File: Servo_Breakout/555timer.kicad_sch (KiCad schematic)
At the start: 14 parts, among them U501 ICM7555xP, U502 TPL0401A-10-Q1

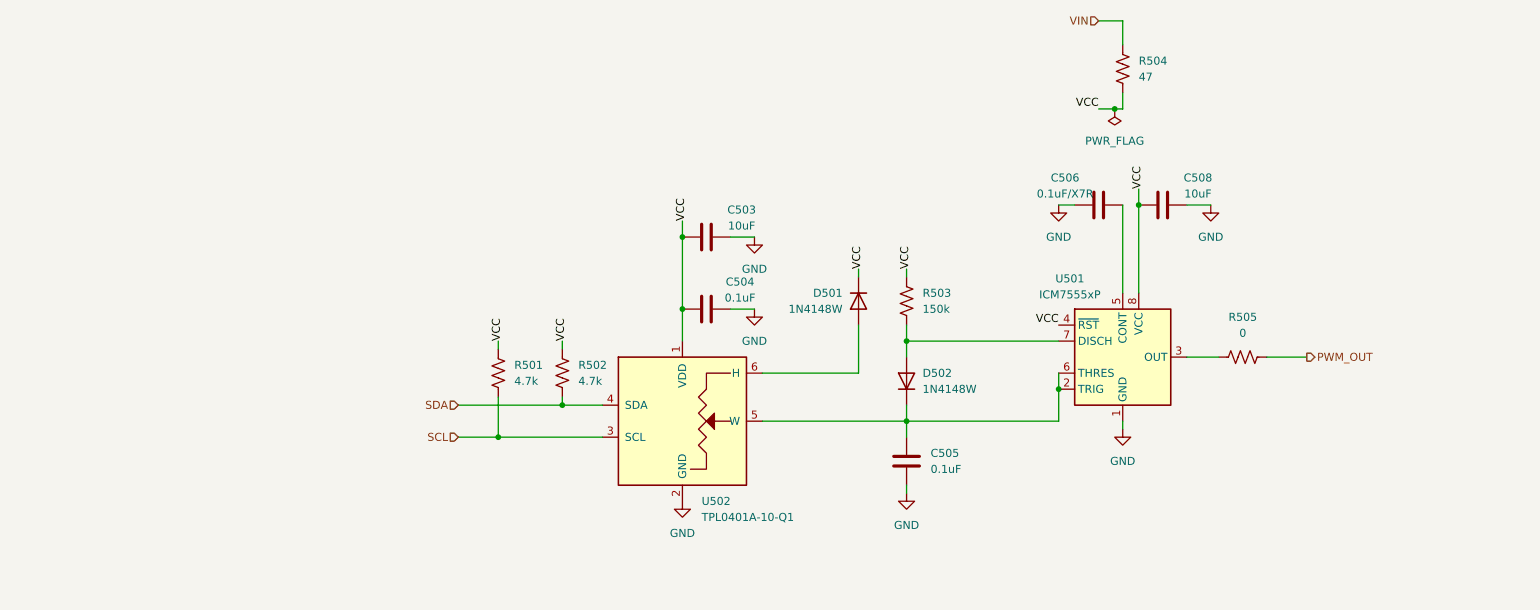
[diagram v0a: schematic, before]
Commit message: simplify 555 timer circuit. update green_led switch to low-side switching
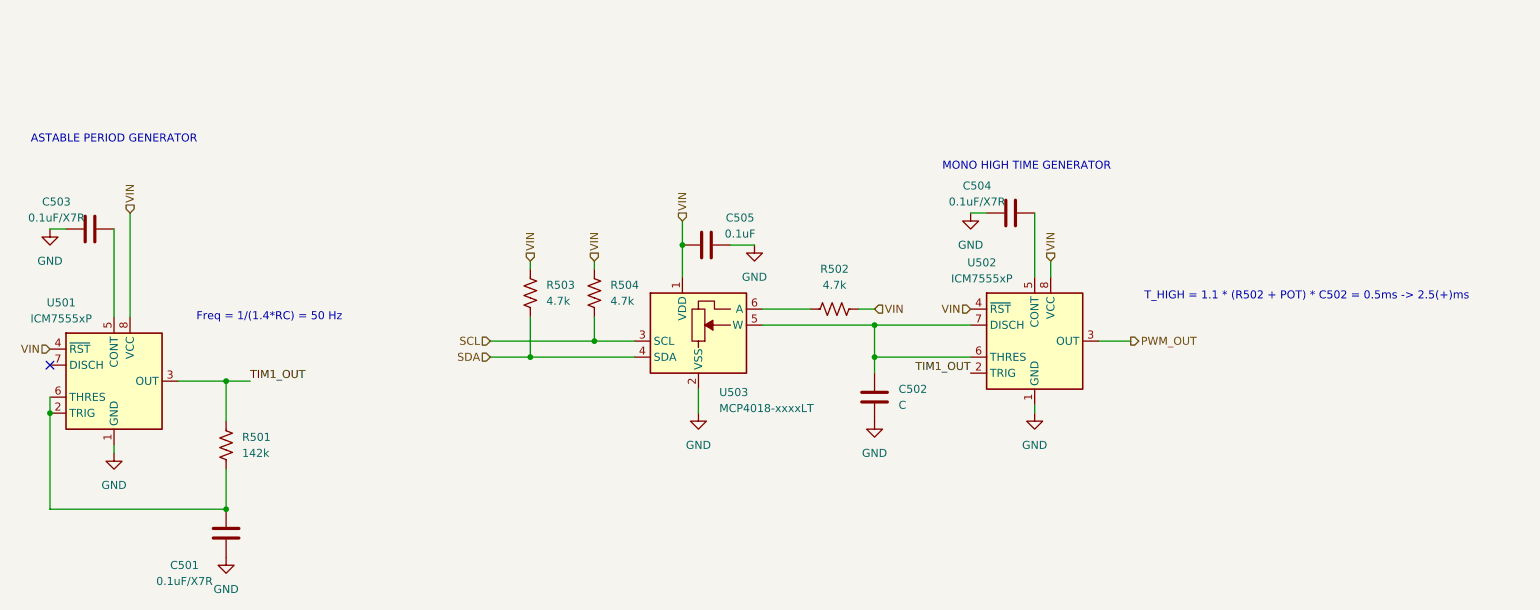
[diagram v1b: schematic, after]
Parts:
- removed C503, C508: 10uF, Capacitor_SMD:C_0805_2012Metric_Pad1.18x1.45mm_HandSolder, symbol Device:C
- removed C505: 0.1uF, Capacitor_SMD:C_0805_2012Metric_Pad1.18x1.45mm_HandSolder, symbol Device:C
- removed D501, D502: 1N4148W, Diode_SMD:D_SOD-123, symbol Diode:1N4148W
- removed R503: 150k, Resistor_SMD:R_0805_2012Metric_Pad1.20x1.40mm_HandSolder, symbol Device:R_US
- removed R504: 47, Resistor_SMD:R_0805_2012Metric_Pad1.20x1.40mm_HandSolder, symbol Device:R_US
- removed R505: 0, Resistor_SMD:R_0603_1608Metric, symbol Device:R_US
- removed U502: TPL0401A-10-Q1, Package_TO_SOT_SMD:Texas_R-PDSO-G6, symbol Potentiometer_Digital:TPL0401A-10-Q1
- added C501, C504: 0.1uF/X7R, Capacitor_SMD:C_0805_2012Metric_Pad1.18x1.45mm_HandSolder, symbol Device:C
- added C502: C, symbol Device:C
- added R501: 142k, symbol Device:R_US
- added R502: 4.7k, symbol Device:R_US
- added U502: ICM7555xP, Package_DIP:DIP-8_W7.62mm, symbol Timer:ICM7555xP
- added U503: MCP4018-xxxxLT, Package_TO_SOT_SMD:SOT-363_SC-70-6, symbol Potentiometer_Digital:MCP4018-xxxxLT
- renumbered C506 to C503, C504 to C505, R501 to R503, R502 to R504
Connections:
- net VCC is gone; now on net VIN: C505.1, R503.1, R504.1, U501.4 (~{RST}), U501.8 (VCC)
- net GND: now also C501.2, C502.2, C504.2, U502.1 (GND), U503.2 (VSS)
- net PWM_OUT: now also U502.3 (OUT)
- net SCL: now also R504.2, U503.3 (SCL); no longer R503.2
- net SDA: now also R503.2, U503.4 (SDA); no longer R504.2
- net VIN: now also R502.2, U502.4 (~{RST}), U502.8 (VCC), U503.1 (VDD)
- net at U501.2 (TRIG), U501.6 (THRES): now also C501.1, R501.2
- net TIM1_OUT: now reaches U501.3 (OUT)
- net TIM1_OUT: now also R501.1, U502.2 (TRIG)
- new net: R502.1, U503.6 (A)
- new net: C502.1, U502.6 (THRES), U502.7 (DISCH), U503.5 (W)
- new net: C504.1, U502.5 (CONT)
- no-connect marks 0 -> 1
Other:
- note added: "ASTABLE PERIOD GENERATOR"
- note added: "Freq = 1/(1.4*RC) = 50 Hz"
- note added: "MONO HIGH TIME GENERATOR"
- note added: "T_HIGH = 1.1 * (R502 + POT) * C502 = 0.5ms -> 2.5(+)ms"
- moved on the sheet: C503, C505, R503, R504, U501

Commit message: completed layout rework for two 555 timers
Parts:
- C502: footprint (none) -> Capacitor_SMD:C_0805_2012Metric_Pad1.18x1.45mm_HandSolder
- R501, R502: footprint (none) -> Resistor_SMD:R_0805_2012Metric_Pad1.20x1.40mm_HandSolder
- R503, R504: footprint Resistor_SMD:R_0603_1608Metric -> Resistor_SMD:R_0805_2012Metric_Pad1.20x1.40mm_HandSolder
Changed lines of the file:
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@@
 			)
 		)
-		(property "Footprint" ""
+		(property "Footprint" "Resistor_SMD:R_0805_2012Metric_Pad1.20x1.40mm_HandSolder"
 			(at 155.194 89.154 90)
 			(effects
@@
 			)
 		)
-		(property "Footprint" "Resistor_SMD:R_0603_1608Metric"
+		(property "Footprint" "Resistor_SMD:R_0805_2012Metric_Pad1.20x1.40mm_HandSolder"
 			(at 107.696 87.884 90)
 			(effects
@@
 			)
 		)
-		(property "Footprint" "Resistor_SMD:R_0603_1608Metric"
+		(property "Footprint" "Resistor_SMD:R_0805_2012Metric_Pad1.20x1.40mm_HandSolder"
 			(at 117.856 87.884 90)
 			(effects
@@
 			)
 		)
-		(property "Footprint" ""
+		(property "Footprint" "Resistor_SMD:R_0805_2012Metric_Pad1.20x1.40mm_HandSolder"
 			(at 59.436 112.014 90)
 			(effects
@@
 			)
 		)
-		(property "Footprint" ""
+		(property "Footprint" "Capacitor_SMD:C_0805_2012Metric_Pad1.18x1.45mm_HandSolder"
 			(at 162.2552 107.95 0)
 			(effects

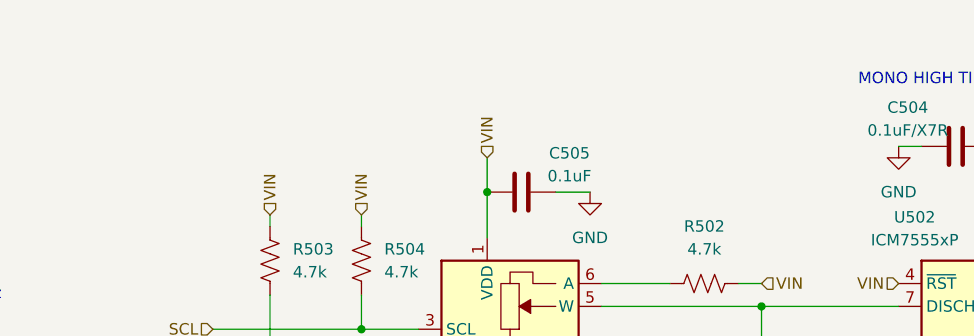
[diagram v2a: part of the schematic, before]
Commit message: more comments on POT in 555 timer circuit and timing calculations
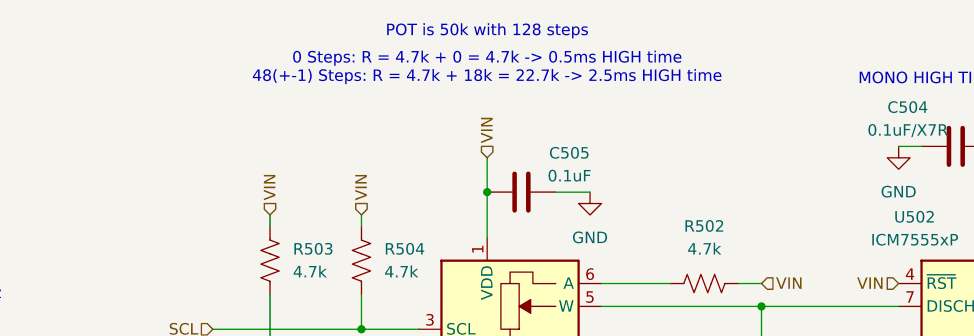
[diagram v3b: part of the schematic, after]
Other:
- note added: "0 Steps: R = 4.7k + 0 = 4.7k -> 0.5ms HIGH time 48(+-1) Steps: R = 4.7k + 18k = 22.7k -> 2.5ms HIGH time"
- note added: "POT is 50k with 128 steps"
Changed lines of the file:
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@@
+		)
+	)
+	(text "POT is 50k with 128 steps"
+		(exclude_from_sim no)
+		(at 130.81 62.23 0)
+		(effects
+			(font
+				(size 1.27 1.27)
+			)
 		)
 	)
@@
 		(effects
 			(font
+				(size 1.27 1.27)
+			)
+		)
+	)
+	(text "0 Steps: R = 4.7k + 0 = 4.7k -> 0.5ms HIGH time\n48(+-1) Steps: R = 4.7k + 18k = 22.7k -> 2.5ms HIGH time"
+		(exclude_from_sim no)
+		(at 130.81 66.294 0)
+		(effects
+			(font

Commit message: servo board final cleanup
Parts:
- added C406: 0.1uF/X7R, Capacitor_SMD:C_0805_2012Metric_Pad1.18x1.45mm_HandSolder, symbol Device:C
- added U404: SN74LVC2G14DBV, Package_TO_SOT_SMD:SOT-23-6, symbol 74xGxx:SN74LVC2G14DBV
- C404: renamed from C502; value C -> 0.1uF
- renumbered C503 to C401, C501 to C402, C505 to C403, C504 to C405, R501 to R401, R503 to R402, R504 to R403, R502 to R404, U501 to U401, U503 to U402, U502 to U403
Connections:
- net GND: now also C406.2, U404.2 (GND)
- net PWM_OUT: now also U404.4 (2Y); no longer U403.3 (OUT)
- net VIN: now also C406.1, U404.5 (V_{CC})
- new net: U403.3 (OUT), U404.1 (1A)
- new net INV_OUT: U404.3 (2A), U404.6 (1Y)

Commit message: servo breakout gerbers
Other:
- company: (none) -> University of Illinois Urbana-Champaign
- title: (none) -> Servo Breakout
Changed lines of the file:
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@@
 	(generator_version "9.0")
 	(paper "A4")
+	(title_block
+		(title "Servo Breakout")
+		(date "2026-03-24")
+		(rev "A")
+		(company "University of Illinois Urbana-Champaign")
+		(comment 4 "Contributors: Noah Breit, Thomas McManamen")
+	)
 	(text "ASTABLE PERIOD GENERATOR"
 		(exclude_from_sim no)
